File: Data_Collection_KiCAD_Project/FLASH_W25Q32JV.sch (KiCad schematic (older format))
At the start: 2 parts

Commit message: Fixed Component Libraries
Changed over from project specific to global libraries.
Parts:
- C?: symbol Data_Collection_KiCAD_Project-rescue:C-Device -> Data_Collection_KiCAD_Project-rescue:C-Device-Data_Collection_KiCAD_Project-rescue
- U?: symbol Data_Collection_KiCAD_Project-rescue:W25Q32JVSS-Memory_Flash -> Data_Collection_KiCAD_Project-rescue:W25Q32JVSS-Memory_Flash-Data_Collection_KiCAD_Project-rescue
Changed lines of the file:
@@
 $Descr A4 11693 8268
 encoding utf-8
-Sheet 6 10
+Sheet 6 9
 Title "W25Q32JVSS Flash Chip"
 Date "2021-10-01"
@@
 $EndDescr
 $Comp
-L Data_Collection_KiCAD_Project-rescue:+3.3V-power #PWR?
+L Data_Collection_KiCAD_Project-rescue:+3.3V-power-Data_Collection_KiCAD_Project-rescue #PWR?
 U 1 1 6161184E
 P 4150 2700
@@
 	4950 2800 4950 2750
 $Comp
-L Data_Collection_KiCAD_Project-rescue:GND-power #PWR?
+L Data_Collection_KiCAD_Project-rescue:GND-power-Data_Collection_KiCAD_Project-rescue #PWR?
 U 1 1 61611855
 P 4950 3600
@@
 Flash Storage Chip
 $Comp
-L Data_Collection_KiCAD_Project-rescue:C-Device C?
+L Data_Collection_KiCAD_Project-rescue:C-Device-Data_Collection_KiCAD_Project-rescue C?
 U 1 1 6161186E
 P 3850 3150
@@
 ~CS
 $Comp
-L Data_Collection_KiCAD_Project-rescue:W25Q32JVSS-Memory_Flash U?
+L Data_Collection_KiCAD_Project-rescue:W25Q32JVSS-Memory_Flash-Data_Collection_KiCAD_Project-rescue U?
 U 1 1 61611848
 P 4950 3200
@@
 $EndComp
 $Comp
-L Data_Collection_KiCAD_Project-rescue:GND-power #PWR?
+L Data_Collection_KiCAD_Project-rescue:GND-power-Data_Collection_KiCAD_Project-rescue #PWR?
 U 1 1 617DF3FC
 P 5500 3450
@@
 Connection ~ 5500 3400
 $Comp
-L Data_Collection_KiCAD_Project-rescue:GND-power #PWR?
+L Data_Collection_KiCAD_Project-rescue:GND-power-Data_Collection_KiCAD_Project-rescue #PWR?
 U 1 1 617DFAF5
 P 3850 3300

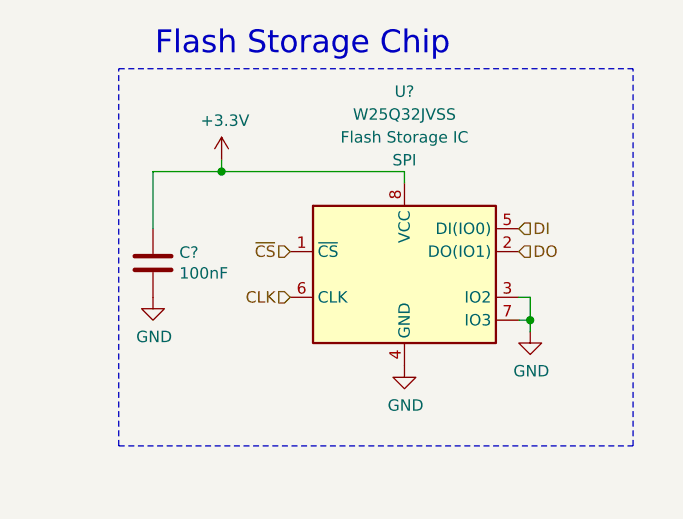
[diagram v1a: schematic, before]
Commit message: footprint and value changes
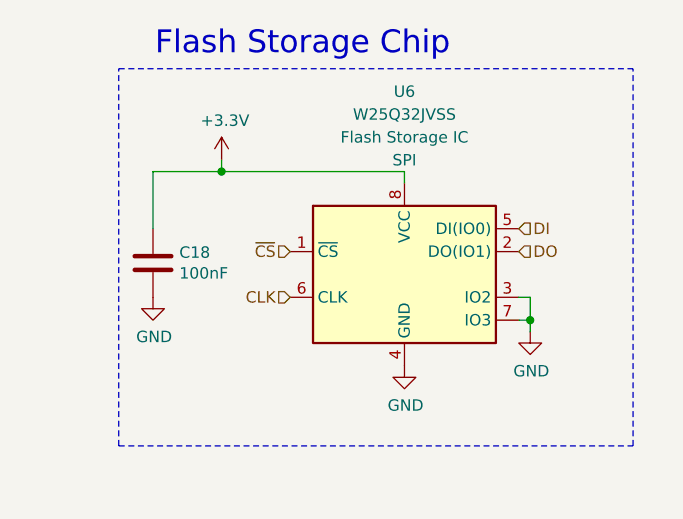
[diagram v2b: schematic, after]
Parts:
- C18: renamed from C?; footprint (none) -> Capacitor_SMD:C_0603_1608Metric
- gave numbers to parts that had none: 1
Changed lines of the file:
@@
 P 4150 2700
 AR Path="/6161184E" Ref="#PWR?"  Part="1"
-AR Path="/615FC266/6161184E" Ref="#PWR?"  Part="1"
-F 0 "#PWR?" H 4150 2550 50  0001 C CNN
+AR Path="/615FC266/6161184E" Ref="#PWR043"  Part="1"
+F 0 "#PWR043" H 4150 2550 50  0001 C CNN
 F 1 "+3.3V" H 4165 2873 50  0000 C CNN
 F 2 "" H 4150 2700 50  0001 C CNN
@@
 P 4950 3600
 AR Path="/61611855" Ref="#PWR?"  Part="1"
-AR Path="/615FC266/61611855" Ref="#PWR?"  Part="1"
-F 0 "#PWR?" H 4950 3350 50  0001 C CNN
+AR Path="/615FC266/61611855" Ref="#PWR044"  Part="1"
+F 0 "#PWR044" H 4950 3350 50  0001 C CNN
 F 1 "GND" H 4955 3427 50  0000 C CNN
 F 2 "" H 4950 3600 50  0001 C CNN
@@
 P 3850 3150
 AR Path="/6161186E" Ref="C?"  Part="1"
-AR Path="/615FC266/6161186E" Ref="C?"  Part="1"
-F 0 "C?" H 3965 3196 50  0000 L CNN
+AR Path="/615FC266/6161186E" Ref="C18"  Part="1"
+F 0 "C18" H 3965 3196 50  0000 L CNN
 F 1 "100nF" H 3965 3105 50  0000 L CNN
-F 2 "" H 3888 3000 50  0001 C CNN
+F 2 "Capacitor_SMD:C_0603_1608Metric" H 3888 3000 50  0001 C CNN
 F 3 "~" H 3850 3150 50  0001 C CNN
 	1    3850 3150
@@
 P 4950 3200
 AR Path="/61611848" Ref="U?"  Part="1"
-AR Path="/615FC266/61611848" Ref="U?"  Part="1"
-F 0 "U?" H 4950 4000 50  0000 C CNN
+AR Path="/615FC266/61611848" Ref="U6"  Part="1"
+F 0 "U6" H 4950 4000 50  0000 C CNN
 F 1 "W25Q32JVSS" H 4950 3900 50  0000 C CNN
 F 2 "Package_SO:SOIC-8_5.23x5.23mm_P1.27mm" H 4950 3200 50  0001 C CNN
@@
 P 5500 3450
 AR Path="/617DF3FC" Ref="#PWR?"  Part="1"
-AR Path="/615FC266/617DF3FC" Ref="#PWR?"  Part="1"
-F 0 "#PWR?" H 5500 3200 50  0001 C CNN
+AR Path="/615FC266/617DF3FC" Ref="#PWR045"  Part="1"
+F 0 "#PWR045" H 5500 3200 50  0001 C CNN
 F 1 "GND" H 5505 3277 50  0000 C CNN
 F 2 "" H 5500 3450 50  0001 C CNN
@@
 P 3850 3300
 AR Path="/617DFAF5" Ref="#PWR?"  Part="1"
-AR Path="/615FC266/617DFAF5" Ref="#PWR?"  Part="1"
-F 0 "#PWR?" H 3850 3050 50  0001 C CNN
+AR Path="/615FC266/617DFAF5" Ref="#PWR042"  Part="1"
+F 0 "#PWR042" H 3850 3050 50  0001 C CNN
 F 1 "GND" H 3855 3127 50  0000 C CNN
 F 2 "" H 3850 3300 50  0001 C CNN

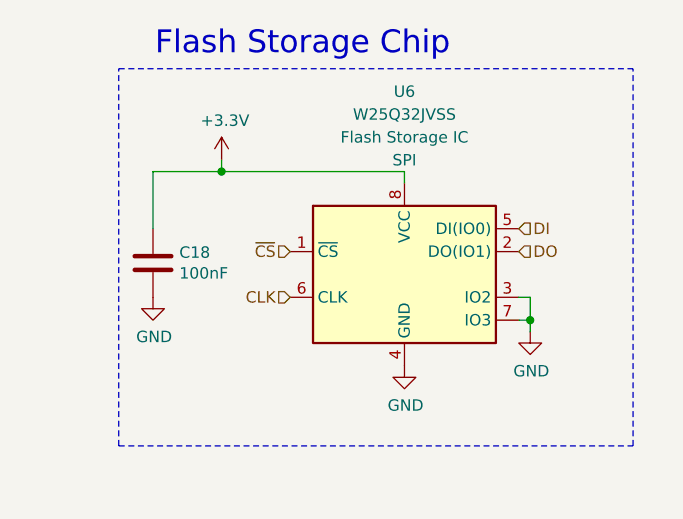
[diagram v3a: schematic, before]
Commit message: footprint changes
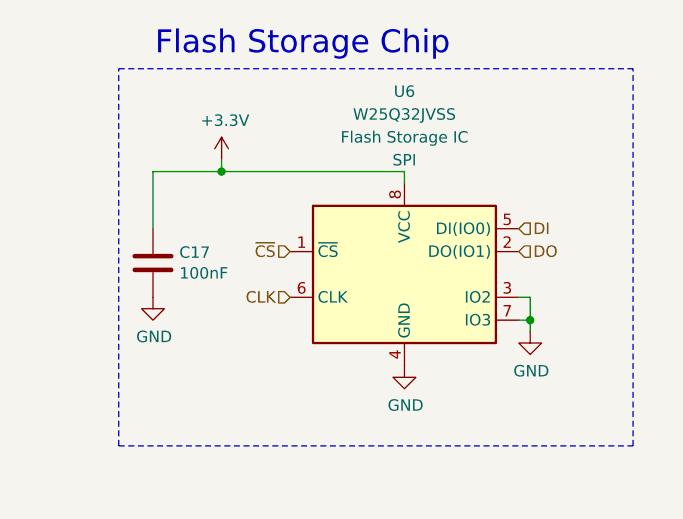
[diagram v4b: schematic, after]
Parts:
- renumbered C18 to C17
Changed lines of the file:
@@
 P 4150 2700
 AR Path="/6161184E" Ref="#PWR?"  Part="1"
-AR Path="/615FC266/6161184E" Ref="#PWR043"  Part="1"
-F 0 "#PWR043" H 4150 2550 50  0001 C CNN
+AR Path="/615FC266/6161184E" Ref="#PWR036"  Part="1"
+F 0 "#PWR036" H 4150 2550 50  0001 C CNN
 F 1 "+3.3V" H 4165 2873 50  0000 C CNN
 F 2 "" H 4150 2700 50  0001 C CNN
@@
 P 4950 3600
 AR Path="/61611855" Ref="#PWR?"  Part="1"
-AR Path="/615FC266/61611855" Ref="#PWR044"  Part="1"
-F 0 "#PWR044" H 4950 3350 50  0001 C CNN
+AR Path="/615FC266/61611855" Ref="#PWR037"  Part="1"
+F 0 "#PWR037" H 4950 3350 50  0001 C CNN
 F 1 "GND" H 4955 3427 50  0000 C CNN
 F 2 "" H 4950 3600 50  0001 C CNN
@@
 P 3850 3150
 AR Path="/6161186E" Ref="C?"  Part="1"
-AR Path="/615FC266/6161186E" Ref="C18"  Part="1"
-F 0 "C18" H 3965 3196 50  0000 L CNN
+AR Path="/615FC266/6161186E" Ref="C17"  Part="1"
+F 0 "C17" H 3965 3196 50  0000 L CNN
 F 1 "100nF" H 3965 3105 50  0000 L CNN
 F 2 "Capacitor_SMD:C_0603_1608Metric" H 3888 3000 50  0001 C CNN
@@
 P 5500 3450
 AR Path="/617DF3FC" Ref="#PWR?"  Part="1"
-AR Path="/615FC266/617DF3FC" Ref="#PWR045"  Part="1"
-F 0 "#PWR045" H 5500 3200 50  0001 C CNN
+AR Path="/615FC266/617DF3FC" Ref="#PWR038"  Part="1"
+F 0 "#PWR038" H 5500 3200 50  0001 C CNN
 F 1 "GND" H 5505 3277 50  0000 C CNN
 F 2 "" H 5500 3450 50  0001 C CNN
@@
 P 3850 3300
 AR Path="/617DFAF5" Ref="#PWR?"  Part="1"
-AR Path="/615FC266/617DFAF5" Ref="#PWR042"  Part="1"
-F 0 "#PWR042" H 3850 3050 50  0001 C CNN
+AR Path="/615FC266/617DFAF5" Ref="#PWR035"  Part="1"
+F 0 "#PWR035" H 3850 3050 50  0001 C CNN
 F 1 "GND" H 3855 3127 50  0000 C CNN
 F 2 "" H 3850 3300 50  0001 C CNN
